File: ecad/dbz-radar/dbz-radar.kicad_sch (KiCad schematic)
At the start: 150 parts, among them J1 B2B-PH-SM4-TB, J2 USB4220-03-0880-C, J3 XF2M-4015-1A, J4 533980271, Q1 Q_PMOS, SW1 SKRPACE010, SW2 SKRPACE010, SW3 1-825027-7, U1 USBLC6-2SC6, U2 TPS61169, U3 MCP738311/2, U4 MAX17048/9, U5 AP2112K-3.3, U6 PCA9554, U7 MAX98357A, U8 ESP32-S3-WROOM-1

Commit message: part placement
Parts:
- removed TP11, TP12, TP15, TP16, TP17, TP18, TP19, TP20, TP21, TP7, TP9: TestPoint_Alt, TestPoint:TestPoint_THTPad_D2.5mm_Drill1.2mm, symbol Connector:TestPoint_Alt
- added J5: Conn_01x12_Pin, Connector_PinHeader_2.54mm:PinHeader_1x12_P2.54mm_Vertical, symbol Connector:Conn_01x12_Pin
- added R72: 0, Resistor_SMD:R_0805_2012Metric_Pad1.20x1.40mm_HandSolder, symbol Device:R_Small_US
- J3: footprint XF2M-4015-1A:XF2M-4015-1A -> XF2M-4015-1A:XF2M-4015-1A_alt
- U8: footprint RF_Module:ESP32-S3-WROOM-1 -> ESP32-S3-WROOM-1:ESP32-S3-WROOM-1_Alt
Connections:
- net EXP_IRQ: now also J5.3 (Pin_3)
- net GND: now also J5.12 (Pin_12)
- net IO35: now also J5.9 (Pin_9)
- net IO36: now also J5.10 (Pin_10)
- net IO37: now also J5.11 (Pin_11)
- net MISO: now also J5.6 (Pin_6)
- net MOSI: now also J5.5 (Pin_5)
- net SCK: now also J5.7 (Pin_7)
- net SCL: now also R72.2; no longer U8.11 (IO18)
- net TXD0: now also J5.8 (Pin_8)
- net ~{BATT_ALRT}: now also J5.2 (Pin_2)
- net BATT_MONITOR-QSTRT: now reaches R14.2, U4.6 (QSTRT)
- net BATT_MONITOR-QSTRT: now also J5.1 (Pin_1)
- net I2C_IO_P6: now reaches U6.11 (P6)
- net I2C_IO_P6: now also J5.4 (Pin_4)
- new net: R72.1, U8.11 (IO18)
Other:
- moved on the sheet: C18, C21, C24, R30, R31, R32, R37, R38, R39, R40, R41, R42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

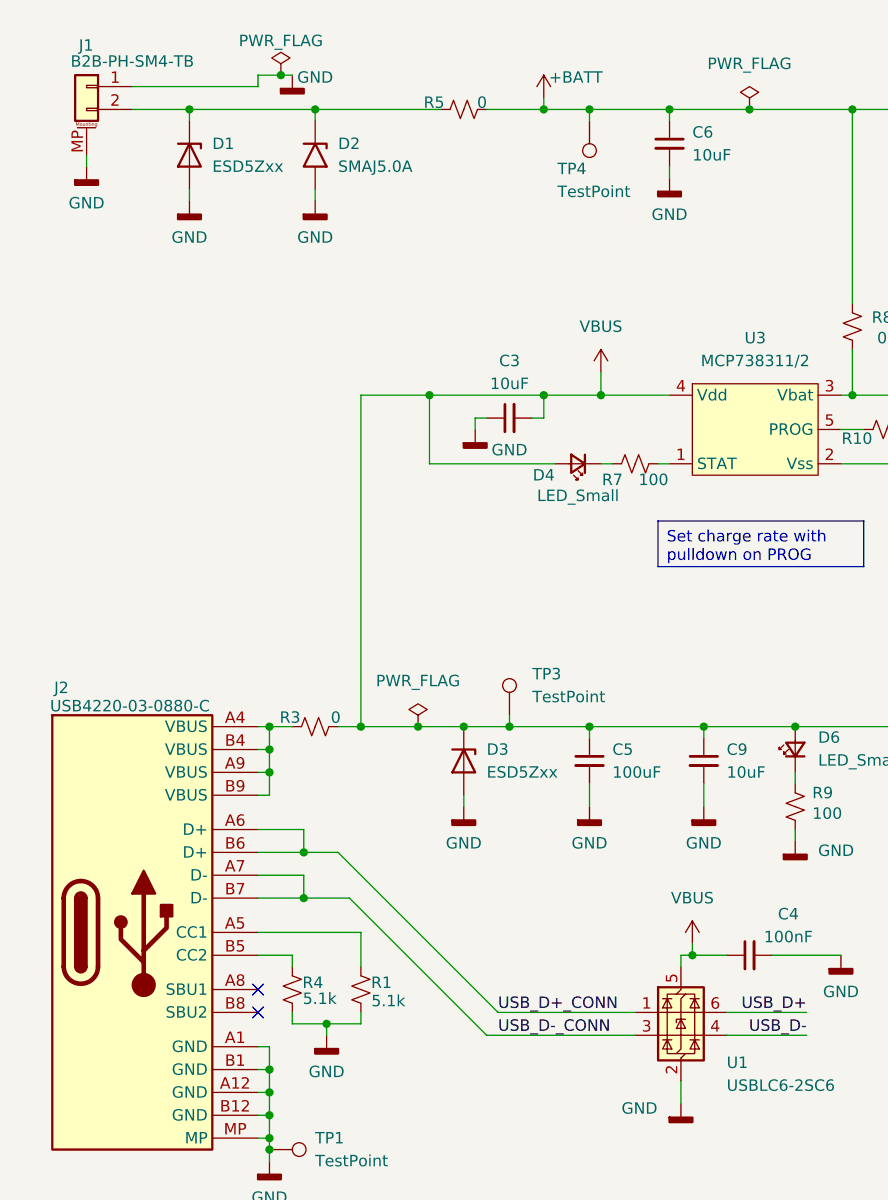
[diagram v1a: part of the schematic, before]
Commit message: start layout of power, USB
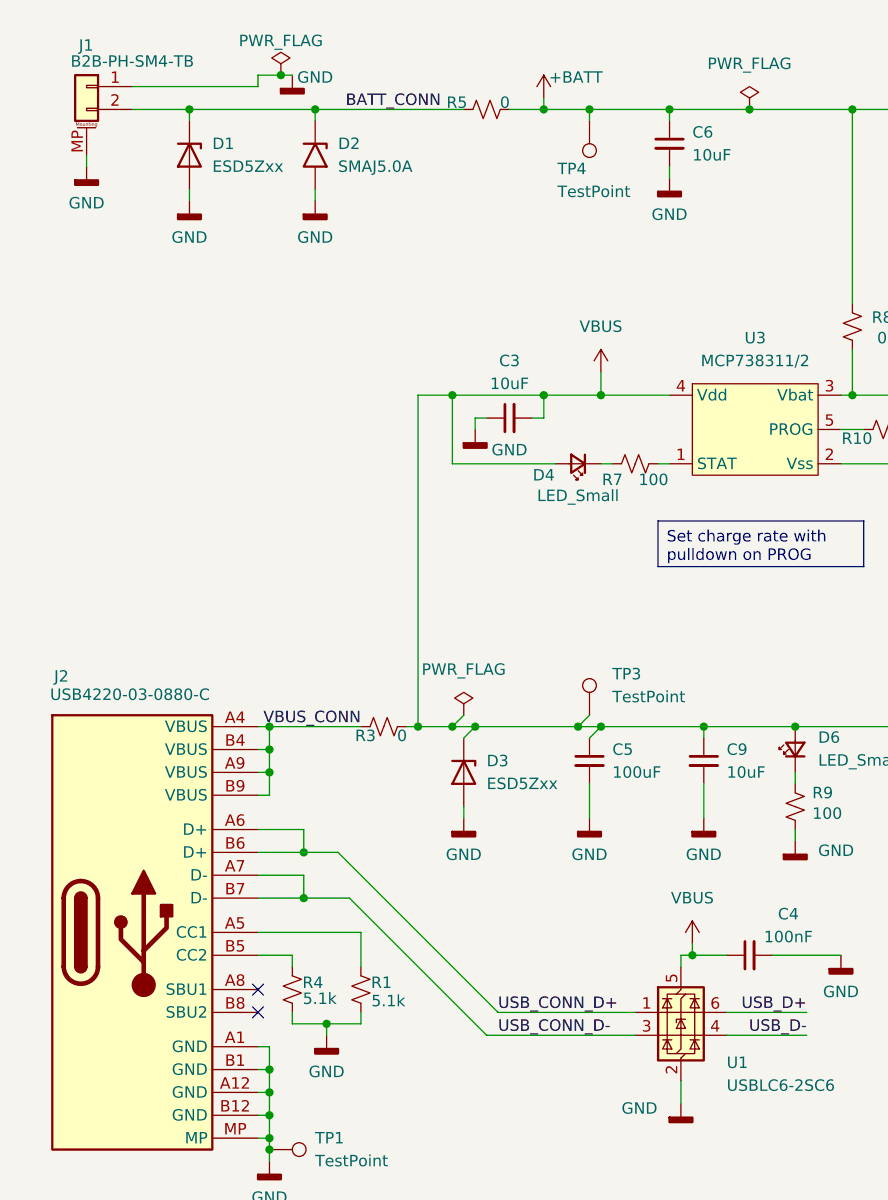
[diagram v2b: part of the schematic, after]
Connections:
- net BATT_CONN: now reaches D1.1 (K), D2.1 (A1), J1.2 (Pin_2), R5.1
- net VBUS_CONN: now reaches J2.A4 (VBUS), J2.A9 (VBUS), J2.B4 (VBUS), J2.B9 (VBUS), R3.1
- net USB_D+_CONN renamed USB_CONN_D+
- net USB_D-_CONN renamed USB_CONN_D-
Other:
- moved on the sheet: D3, R3, R5, TP3

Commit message: route USB, VBUS
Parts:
- removed C4: 100nF, Capacitor_SMD:C_0805_2012Metric_Pad1.18x1.45mm_HandSolder, symbol Device:C_Small
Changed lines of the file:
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@@
 	)
 	(junction
-		(at 86.36 115.57)
-		(diameter 0)
-		(color 0 0 0 0)
-	)
-	(junction
 		(at 39.37 130.81)
 		(diameter 0)
@@
 	(wire
 		(pts
-			(xy 86.36 115.57) (xy 90.17 115.57)
-		)
-		(stroke
-			(width 0)
-			(type default)
-		)
-	)
-	(wire
-		(pts
 			(xy 181.61 176.53) (xy 181.61 179.07)
 		)
@@
 	(wire
 		(pts
-			(xy 95.25 115.57) (xy 102.87 115.57)
-		)
-		(stroke
-			(width 0)
-			(type default)
-		)
-	)
-	(wire
-		(pts
 			(xy 154.94 19.05) (xy 154.94 17.78)
 		)
@@
 	(wire
 		(pts
-			(xy 85.09 115.57) (xy 85.09 116.84)
-		)
-		(stroke
-			(width 0)
-			(type default)
-		)
-	)
-	(wire
-		(pts
 			(xy 143.51 90.17) (xy 149.86 90.17)
 		)
@@
 	(wire
 		(pts
-			(xy 86.36 114.3) (xy 86.36 115.57)
+			(xy 85.09 115.57) (xy 85.09 116.84)
 		)
 		(stroke
@@
 		)
 	)
-	(wire
-		(pts
-			(xy 85.09 115.57) (xy 86.36 115.57)
-		)
-		(stroke
-			(width 0)
-			(type default)
-		)
-	)
 	(image
 		(at 292.1 110.49)
@@
 	(symbol
 		(lib_id "power:VBUS")
-		(at 86.36 114.3 0)
+		(at 85.09 115.57 0)
 		(unit 1)
 		(exclude_from_sim no)
@@
 		(fields_autoplaced yes)
 		(property "Reference" "#PWR013"
-			(at 86.36 118.11 0)
+			(at 85.09 119.38 0)
 			(effects
 				(font
@@
 		)
 		(property "Value" "VBUS"
-			(at 86.36 109.22 0)
+			(at 85.09 110.49 0)
 			(effects
 				(font
@@
 		)
 		(property "Footprint" ""
-			(at 86.36 114.3 0)
+			(at 85.09 115.57 0)
 			(effects
 				(font
@@
 		)
 		(property "Datasheet" ""
-			(at 86.36 114.3 0)
+			(at 85.09 115.57 0)
 			(effects
 				(font
@@
 		)
 		(property "Description" "Power symbol creates a global label with name \"VBUS\""
-			(at 86.36 114.3 0)
+			(at 85.09 115.57 0)
 			(effects
 				(font
@@
 	)
 	(symbol
-		(lib_id "power:GNDD")
-		(at 102.87 115.57 0)
-		(unit 1)
-		(exclude_from_sim no)
-		(in_bom yes)
-		(on_board yes)
-		(dnp no)
-		(property "Reference" "#PWR021"
-			(at 102.87 121.92 0)
-			(effects
-				(font
-					(size 1.27 1.27)
-				)
-				(hide yes)
-			)
-		)
-		(property "Value" "GND"
-			(at 102.87 119.634 0)
-			(effects
-				(font
-					(size 1.27 1.27)
-				)
-			)
-		)
-		(property "Footprint" ""
-			(at 102.87 115.57 0)
-			(effects
-				(font
-					(size 1.27 1.27)
-				)
-				(hide yes)
-			)
-		)
-		(property "Datasheet" ""
-			(at 102.87 115.57 0)
-			(effects
-				(font
-					(size 1.27 1.27)
-				)
-				(hide yes)
-			)
-		)
-		(property "Description" "Power symbol creates a global label with name \"GNDD\" , digital ground"
-			(at 102.87 115.57 0)
-			(effects
-				(font
-					(size 1.27 1.27)
-				)
-				(hide yes)
-			)
-		)
-		(pin "1"
-		)
-		(instances
-			(project "dbz-radar"
-				(path "/71bbee33-6224-4636-be0a-89c36c1c9290"
-					(reference "#PWR021")
-					(unit 1)
-				)
-			)
-		)
-	)
-	(symbol
 		(lib_id "Regulator_Linear:AP2112K-3.3")
 		(at 187.96 92.71 0)
@@
 					(unit 1)
 				)
-			)
-		)
-	)
-	(symbol
-		(lib_id "Device:C_Small")
-		(at 92.71 115.57 90)
-		(unit 1)
-		(exclude_from_sim no)
-		(in_bom yes)
-		(on_board yes)
-		(dnp no)
-		(property "Reference" "C4"
-			(at 97.028 110.998 90)
-			(effects
-				(font
-					(size 1.27 1.27)
-				)
-			)
-		)
-		(property "Value" "100nF"
-			(at 97.028 113.538 90)
-			(effects
-				(font
-					(size 1.27 1.27)
-				)
-			)
-		)
-		(property "Footprint" "Capacitor_SMD:C_0805_2012Metric_Pad1.18x1.45mm_HandSolder"
-			(at 92.71 115.57 0)
-			(effects
-				(font
-					(size 1.27 1.27)
-				)
-				(hide yes)
-			)
-		)
-		(property "Datasheet" "~"
-			(at 92.71 115.57 0)
-			(effects
-				(font
-					(size 1.27 1.27)
-				)
-				(hide yes)
-			)
-		)
-		(property "Description" "Unpolarized capacitor, small symbol"
-			(at 92.71 115.57 0)
-			(effects
-				(font
-					(size 1.27 1.27)
-				)
-				(hide yes)
-			)
-		)
-		(pin "1"
-		)
-		(pin "2"
-		)
-		(instances
-			(project "dbz-radar"
-				(path "/71bbee33-6224-4636-be0a-89c36c1c9290"
-					(reference "C4")
-					(unit 1)
-				)

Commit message: first pass layout
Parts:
- J5: footprint Connector_PinHeader_2.54mm:PinHeader_1x12_P2.54mm_Vertical -> Connector_PinHeader_2.54mm:PinHeader_1x14_P2.54mm_Vertical; symbol Connector:Conn_01x12_Pin -> Connector:Conn_01x14_Pin
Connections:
- net +3V3: now also R32.2; no longer R32.1, SW1.2
- net BATT_MONITOR-QSTRT: now also J5.10 (Pin_10); no longer J5.1 (Pin_1)
- net CS: now also J5.5 (Pin_5)
- net EXP_IRQ: now also J5.12 (Pin_12); no longer J5.3 (Pin_3)
- net GND: now also J5.14 (Pin_14); no longer J5.12 (Pin_12)
- net I2C_IO_P6: now also J5.11 (Pin_11); no longer J5.4 (Pin_4)
- net IO35: now also J5.8 (Pin_8); no longer J5.9 (Pin_9)
- net IO36: now also J5.7 (Pin_7); no longer J5.10 (Pin_10)
- net IO37: now also J5.6 (Pin_6); no longer J5.11 (Pin_11)
- net MISO: now also J5.3 (Pin_3); no longer J5.6 (Pin_6)
- net MOSI: now also J5.4 (Pin_4); no longer J5.5 (Pin_5)
- net SCK: now also J5.2 (Pin_2); no longer J5.7 (Pin_7)
- net TXD0: now also J5.1 (Pin_1); no longer J5.8 (Pin_8)
- net ~{BATT_ALRT}: now also J5.9 (Pin_9); no longer J5.2 (Pin_2)
- net ~{RESET}: now also R32.1, SW1.2; no longer R32.2
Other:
- moved on the sheet: C18, R32, SW1

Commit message: finalize layout
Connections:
- net USB_CONN_D+ is gone; now on net USB_D+: J2.A6 (D+), J2.B6 (D+), U1.1 (I/O1)
- net USB_CONN_D- is gone; now on net USB_D-: J2.A7 (D-), J2.B7 (D-), U1.3 (I/O2)
- net +3V3: now also J5.13 (Pin_13)
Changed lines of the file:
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@@
 	(wire
 		(pts
-			(xy 207.01 201.93) (xy 232.41 201.93)
+			(xy 207.01 201.93) (xy 237.49 201.93)
 		)
 		(stroke
@@
 	(wire
 		(pts
+			(xy 237.49 199.39) (xy 237.49 201.93)
+		)
+		(stroke
+			(width 0)
+			(type default)
+		)
+	)
+	(wire
+		(pts
 			(xy 154.94 19.05) (xy 154.94 17.78)
 		)
@@
 		)
 	)
+	(label "USB_D-"
+		(at 72.39 124.46 0)
+		(effects
+			(font
+				(size 1.27 1.27)
+			)
+			(justify left bottom)
+		)
+	)
 	(label "VSYNC"
 		(at 172.72 207.01 0)
@@
 		)
 	)
-	(label "USB_CONN_D+"
-		(at 64.77 121.92 0)
-		(effects
-			(font
-				(size 1.27 1.27)
-			)
-			(justify left bottom)
-		)
-	)
 	(label "BATT_MONITOR-QSTRT"
 		(at 232.41 194.31 180)
@@
 		)
 	)
-	(label "EXP_IRQ"
-		(at 278.13 238.76 180)
+	(label "USB_D+"
+		(at 72.39 121.92 0)
 		(effects
 			(font
 				(size 1.27 1.27)
 			)
-			(justify right bottom)
+			(justify left bottom)
 		)
 	)
-	(label "SCK"
-		(at 232.41 173.99 180)
+	(label "EXP_IRQ"
+		(at 278.13 238.76 180)
 		(effects
 			(font
@@
 		)
 	)
-	(label "USB_CONN_D-"
-		(at 64.77 124.46 0)
+	(label "SCK"
+		(at 232.41 173.99 180)
 		(effects
 			(font
 				(size 1.27 1.27)
 			)
-			(justify left bottom)
+			(justify right bottom)
 		)
 	)
@@
 					(unit 1)
 				)
+			)
+		)
+	)
+	(symbol
+		(lib_id "power:+3V3")
+		(at 237.49 199.39 0)
+		(unit 1)
+		(exclude_from_sim no)
+		(in_bom yes)
+		(on_board yes)
+		(dnp no)
+		(fields_autoplaced yes)
+		(property "Reference" "#PWR021"
+			(at 237.49 203.2 0)
+			(effects
+				(font
+					(size 1.27 1.27)
+				)
+				(hide yes)
+			)
+		)
+		(property "Value" "+3V3"
+			(at 237.49 194.31 0)
+			(effects
+				(font
+					(size 1.27 1.27)
+				)
+			)
+		)
+		(property "Footprint" ""
+			(at 237.49 199.39 0)
+			(effects
+				(font
+					(size 1.27 1.27)
+				)
+				(hide yes)
+			)
+		)
+		(property "Datasheet" ""
+			(at 237.49 199.39 0)
+			(effects
+				(font
+					(size 1.27 1.27)
+				)
+				(hide yes)
+			)
+		)
+		(property "Description" "Power symbol creates a global label with name \"+3V3\""
+			(at 237.49 199.39 0)
+			(effects
+				(font
+					(size 1.27 1.27)
+				)
+				(hide yes)
+			)
+		)
+		(pin "1"
+		)
+		(instances
+			(project "dbz-radar"
+				(path "/71bbee33-6224-4636-be0a-89c36c1c9290"
+					(reference "#PWR021")
+					(unit 1)
+				)

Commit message: add all 3D shapes, add helpful text so silkscreen
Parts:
- removed D2: SMAJ5.0A, Diode_SMD:D_SMA, symbol Diode:SMAJ5.0A
- J5, R16, R18, R24, R26, R28: now not fitted
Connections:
- net EXP_IRQ renamed ~{EXP_IRQ}
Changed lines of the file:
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@@
 	)
 	(junction
-		(at 44.45 21.59)
-		(diameter 0)
-		(color 0 0 0 0)
-	)
-	(junction
 		(at 87.63 173.99)
 		(diameter 0)
@@
 	(wire
 		(pts
-			(xy 44.45 21.59) (xy 60.96 21.59)
-		)
-		(stroke
-			(width 0)
-			(type default)
-		)
-	)
-	(wire
-		(pts
 			(xy 172.72 229.87) (xy 184.15 229.87)
 		)
@@
 	(wire
 		(pts
-			(xy 30.48 21.59) (xy 44.45 21.59)
+			(xy 30.48 21.59) (xy 60.96 21.59)
 		)
 		(stroke
@@
 	(wire
 		(pts
-			(xy 44.45 30.48) (xy 44.45 31.75)
-		)
-		(stroke
-			(width 0)
-			(type default)
-		)
-	)
-	(wire
-		(pts
 			(xy 172.72 265.43) (xy 184.15 265.43)
 		)
@@
 	(wire
 		(pts
-			(xy 44.45 21.59) (xy 44.45 22.86)
-		)
-		(stroke
-			(width 0)
-			(type default)
-		)
-	)
-	(wire
-		(pts
 			(xy 172.72 260.35) (xy 184.15 260.35)
 		)
@@
 		)
 	)
-	(label "EXP_IRQ"
+	(label "~{EXP_IRQ}"
 		(at 232.41 199.39 180)
 		(effects
@@
 		)
 	)
-	(label "EXP_IRQ"
+	(label "~{EXP_IRQ}"
 		(at 278.13 238.76 180)
 		(effects
@@
 		(in_bom yes)
 		(on_board yes)
-		(dnp no)
+		(dnp yes)
 		(property "Reference" "R26"
 			(at 224.282 235.966 90)
@@
 		(in_bom yes)
 		(on_board yes)
-		(dnp no)
+		(dnp yes)
 		(property "Reference" "J5"
 			(at 202.692 167.132 0)
@@
 		(in_bom yes)
 		(on_board yes)
-		(dnp no)
+		(dnp yes)
 		(property "Reference" "R18"
 			(at 159.512 194.056 90)
@@
 	)
 	(symbol
-		(lib_id "Diode:SMAJ5.0A")
-		(at 44.45 26.67 270)
-		(unit 1)
-		(exclude_from_sim no)
-		(in_bom yes)
-		(on_board yes)
-		(dnp no)
-		(fields_autoplaced yes)
-		(property "Reference" "D2"
-			(at 46.99 25.3999 90)
-			(effects
-				(font
-					(size 1.27 1.27)
-				)
-				(justify left)
-			)
-		)
-		(property "Value" "SMAJ5.0A"
-			(at 46.99 27.9399 90)
-			(effects
-				(font
-					(size 1.27 1.27)
-				)
-				(justify left)
-			)
-		)
-		(property "Footprint" "Diode_SMD:D_SMA"
-			(at 39.37 26.67 0)
-			(effects
-				(font
-					(size 1.27 1.27)
-				)
-				(hide yes)
-			)
-		)
-		(property "Datasheet" "https://www.littelfuse.com/media?resourcetype=datasheets&itemid=75e32973-b177-4ee3-a0ff-cedaf1abdb93&filename=smaj-datasheet"
-			(at 44.45 25.4 0)
-			(effects
-				(font
-					(size 1.27 1.27)
-				)
-				(hide yes)
-			)
-		)
-		(property "Description" "400W unidirectional Transient Voltage Suppressor, 5.0Vr, SMA(DO-214AC)"
-			(at 44.45 26.67 0)
-			(effects
-				(font
-					(size 1.27 1.27)
-				)
-				(hide yes)
-			)
-		)
-		(pin "1"
-		)
-		(pin "2"
-		)
-		(instances
-			(project "dbz-radar"
-				(path "/71bbee33-6224-4636-be0a-89c36c1c9290"
-					(reference "D2")
-					(unit 1)
-				)
-			)
-		)
-	)
-	(symbol
 		(lib_id "Device:R_Small_US")
 		(at 323.85 182.88 90)
@@
 		(in_bom yes)
 		(on_board yes)
-		(dnp no)
+		(dnp yes)
 		(property "Reference" "R24"
 			(at 227.076 242.824 0)
@@
 		(in_bom yes)
 		(on_board yes)
-		(dnp no)
+		(dnp yes)
 		(property "Reference" "R16"
 			(at 145.796 194.056 90)
@@
 		(in_bom yes)
 		(on_board yes)
-		(dnp no)
+		(dnp yes)
 		(property "Reference" "R28"
 			(at 236.728 225.044 90)
@@
 					(unit 1)
 				)
-			)
-		)
-	)
-	(symbol
-		(lib_id "power:GNDD")
-		(at 44.45 31.75 0)
-		(unit 1)
-		(exclude_from_sim no)
-		(in_bom yes)
-		(on_board yes)
-		(dnp no)
-		(property "Reference" "#PWR09"
-			(at 44.45 38.1 0)
-			(effects
-				(font
-					(size 1.27 1.27)
-				)
-				(hide yes)
-			)
-		)
-		(property "Value" "GND"
-			(at 44.45 35.814 0)
-			(effects
-				(font
-					(size 1.27 1.27)
-				)
-			)
-		)
-		(property "Footprint" ""
-			(at 44.45 31.75 0)
-			(effects
-				(font
-					(size 1.27 1.27)
-				)
-				(hide yes)
-			)
-		)
-		(property "Datasheet" ""
-			(at 44.45 31.75 0)
-			(effects
-				(font
-					(size 1.27 1.27)
-				)
-				(hide yes)
-			)
-		)
-		(property "Description" "Power symbol creates a global label with name \"GNDD\" , digital ground"
-			(at 44.45 31.75 0)
-			(effects
-				(font
-					(size 1.27 1.27)
-				)
-				(hide yes)
-			)
-		)
-		(pin "1"
-		)
-		(instances
-			(project "dbz-radar"
-				(path "/71bbee33-6224-4636-be0a-89c36c1c9290"
-					(reference "#PWR09")
-					(unit 1)
-				)

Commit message: add part numbers to all components
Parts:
- C1, C11, C14, C16, C19, C3, C6, C9: LCSC (none) -> C380347; MFG (none) -> CCTC; MFG PN (none) -> TCC0805X7R106K160FT; Package (none) -> 0805
- C10, C18, C8: LCSC (none) -> C52923; MFG (none) -> Samsung Electro-Mechanics; MFG PN (none) -> CL05A105KA5NQNC; Package (none) -> 0805
- C12, C13, C15, C17, C2, C20, C24, C7: LCSC (none) -> C49678; MFG (none) -> YAGEO; MFG PN (none) -> CC0805KRX7R9BB104; Package (none) -> 0805
- C21: LCSC (none) -> C15008; MFG (none) -> Samsung Electro-Mechanics; MFG PN (none) -> CL31A107MQHNNNE; Package (none) -> 1206
- C22, C23, R34, R36: LCSC (none) -> DNI; MFG (none) -> DNI; MFG PN (none) -> DNI; Package (none) -> 0805; now not fitted
- C5: footprint Capacitor_SMD:C_0805_2012Metric_Pad1.18x1.45mm_HandSolder -> Capacitor_SMD:C_1206_3216Metric_Pad1.33x1.80mm_HandSolder; LCSC (none) -> C15008; MFG (none) -> Samsung Electro-Mechanics; MFG PN (none) -> CL31A107MQHNNNE; Package (none) -> 1206
- D1, D3: LCSC (none) -> C502546; MFG (none) -> MDD(Microdiode Semiconductor); MFG PN (none) -> ESD5Z5V0; Package (none) -> SOD-523
- D4, D6, D8, D9: LCSC (none) -> C2295; MFG (none) -> Hubei KENTO Elec; MFG PN (none) -> KT-0805R; Package (none) -> 0805
- D5, D7: LCSC (none) -> C77337; MFG (none) -> Jiangsu Changjing Electronics Technology Co., Ltd.; MFG PN (none) -> MBR0540; Package (none) -> SOD-123; now left out of the parts list
- J1: LCSC (none) -> C160352; MFG (none) -> JST; MFG PN (none) -> B2B-PH-SM4-TB; Package (none) -> 2-pin, 2.00mm pitch, vertical connector
- J2: LCSC (none) -> C41730496; MFG (none) -> Global Connector Technology; MFG PN (none) -> USB4220-03-0880-C; Package (none) -> Vertical USB-C, 8.80mm height
- J3: LCSC (none) -> C225713; MFG (none) -> Omron Electronics; MFG PN (none) -> XF2M-4015-1A; Package (none) -> Surface mount, 0.5mm, 40 pin, double-sided contact ffc conn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
- J4: LCSC (none) -> C122410; MFG (none) -> Molex; MFG PN (none) -> 533980271; Package (none) -> Surface mount, 2-pin, 1.25m pitch, vertical
- J5: value Conn_01x12_Pin -> DNI; LCSC (none) -> DNI; MFG (none) -> DNI; MFG PN (none) -> DNI; Package (none) -> DNI
- L1: LCSC (none) -> C82157; MFG (none) -> TDK; MFG PN (none) -> MLZ2012N6R8LT000; Package (none) -> 0805
- Q1: LCSC (none) -> C15127; MFG (none) -> AO3401A; MFG PN (none) -> Alpha & Omega Semicon; Package (none) -> SOT-23
- R1, R10, R11, R12, R2, R30, R31, R32, R33, R35, R4, R70, R71: LCSC (none) -> C27834; MFG (none) -> UNI-ROYAL(Uniroyal Elec); MFG PN (none) -> 0805W8F5101T5E; Package (none) -> 0805
- R13, R14, R15, R17, R19, R20, R21, R22, R23, R25, R27, R29, R3, R37, R38, R39, R40, R41, R42, R43, R44, R45, R46, R47, R48, R49, R5, R50, R51, R52, R53, R54, R55, R56, R57, R58, R59, R60, R61, R62, R63, R64, R65, R66, R67, R68, R69, R7, R72, R8, R9: LCSC (none) -> C17477; MFG (none) -> UNI-ROYAL(Uniroyal Elec); MFG PN (none) -> 0805W8F0000T5E; Package (none) -> 0805
- R16, R18, R24, R26, R28: LCSC (none) -> DNI; MFG (none) -> DNI; MFG PN (none) -> DNI; Package (none) -> 0805
- R6: value 8.2 -> 10; LCSC (none) -> C17477; MFG (none) -> UNI-ROYAL(Uniroyal Elec); MFG PN (none) -> 0805W8F0000T5E; Package (none) -> 0805
- SW1, SW2: LCSC (none) -> C139797; MFG (none) -> ALPSALPINE; MFG PN (none) -> SKRPACE010; Package (none) -> 4-pin, surface mount
- SW3: LCSC (none) -> C592923; MFG (none) -> TE Connectivity; MFG PN (none) -> 1-825027-7; Package (none) -> 4-pin, through hole
- TP1, TP10, TP14, TP2, TP3, TP4, TP5, TP6, TP8: now left out of the parts list
- U1: LCSC (none) -> C5180249; MFG (none) -> ElecSuper; MFG PN (none) -> USBLC6-2SC6; Package (none) -> SOT-23-6
- U2: LCSC (none) -> C71045; MFG (none) -> Texas Instruments; MFG PN (none) -> TPS61169; Package (none) -> SC-70-5
- U3: LCSC (none) -> C424093; MFG (none) -> Microchip Tech; MFG PN (none) -> MCP73831T-2ACI/OT; Package (none) -> SOT-23-5
- U4: LCSC (none) -> C7497002; MFG (none) -> Analog Devices Inc./Maxim Integrated; MFG PN (none) -> MAX17048X+T10; Package (none) -> WLP-8(0.9x1.8)
- U5: LCSC (none) -> C22365427; MFG (none) -> MSKSEMI; MFG PN (none) -> AP2112K-3.3TRG1(MS); Package (none) -> SOT-23-5
- U6: LCSC (none) -> C2873588; MFG (none) -> Texas Instruments; MFG PN (none) -> PCA9554PWR; Package (none) -> TSSOP-16
- U7: LCSC (none) -> C910544; MFG (none) -> Analog Devices Inc./Maxim Integrated; MFG PN (none) -> MAX98357A; Package (none) -> TQFN-16-EP(3x3)
- U8: value ESP32-S3-WROOM-1 -> ESP32-S3-WROOM-1-N16R8; LCSC (none) -> C2913202; MFG (none) -> Espressif Systems; MFG PN (none) -> ESP32-S3-WROOM-1-N16R8; Package (none) -> Surface mount RF module

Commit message: add designer info to schematic
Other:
- company: (none) -> Extra Long Division
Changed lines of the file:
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@@
 	(title_block
 		(title "Dragon Ball Radar")
+		(date "2026-07-20")
 		(rev "0.1.0")
+		(company "Extra Long Division")
+		(comment 1 "extralongdivision.com")
+		(comment 2 "Creative Commons Attribution-ShareAlike 4.0 International")
 	)
 	(text "HD40015C40"
